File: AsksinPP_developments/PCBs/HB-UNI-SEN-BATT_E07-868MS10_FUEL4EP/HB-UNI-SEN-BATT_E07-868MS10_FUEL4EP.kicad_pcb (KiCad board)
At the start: 2 copper layers, 75 x 75 mm, 30 parts, among them J1 Conn_01x02, J10 charge, J11 ePaper connector, J2 Conn_01x02, J3 Conn_01x02, J4 Conn_01x02, J5 ISP Programmer, J6 Conn_01x04, J7 Conn_01x04, J8 Conn_01x04, J9 Conn_01x04, Q1 IRLU024N, SW1 config button

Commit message: Updates of PCBs/HB-UNI-SEN-BATT_FUEL4EP and HB-UNI-SEN-BATT_E07-868MS10_FUEL4EP
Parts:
- BT1, BT2: footprint FUEL4EP:BATTERY_HOLDER_GOOBAY_AA -> FUEL4EP:BatteryHolder_Keystone_2460_1xAA
- J11: footprint Connector_PinHeader_2.54mm:PinHeader_1x08_P2.54mm_Vertical -> FUEL4EP:PinPads_1x08_P2.00mm_Vertical
- moved BT1 55.3 mm to (164.5, 86.9), turned to 270 degrees
- moved BT2 55.0 mm to (112.4, 138.9), turned to 90 degrees
- moved J11 3.93 mm to (127.9, 130.7)
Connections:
- net Net-(BT1-Pad2) renamed /conBAT
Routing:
- net /D6: track 33.9 -> 47.5 mm, vias 0 -> 2
- net /D7: track 37.6 -> 31.9 mm
- net /SDA: track 101.2 -> 104.3 mm
- net /D5: track 47.5 -> 49.8 mm
- net /SCK: track 76.5 -> 74.6 mm
- net /MISO: track 88.6 -> 87.0 mm
- net /conBAT: track 53.5 -> 52.1 mm
- net /RSET: track 94.8 -> 96.0 mm
- net /MOSI: track 68.1 -> 67.5 mm
- net /plusBAT: track 19.4 -> 19.9 mm
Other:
- board text added: "config"
- board text added: "cut JP2 for accus"
- board text removed: "4"
- board text removed: "5"
- board text removed: "cut JP2 for akkus"

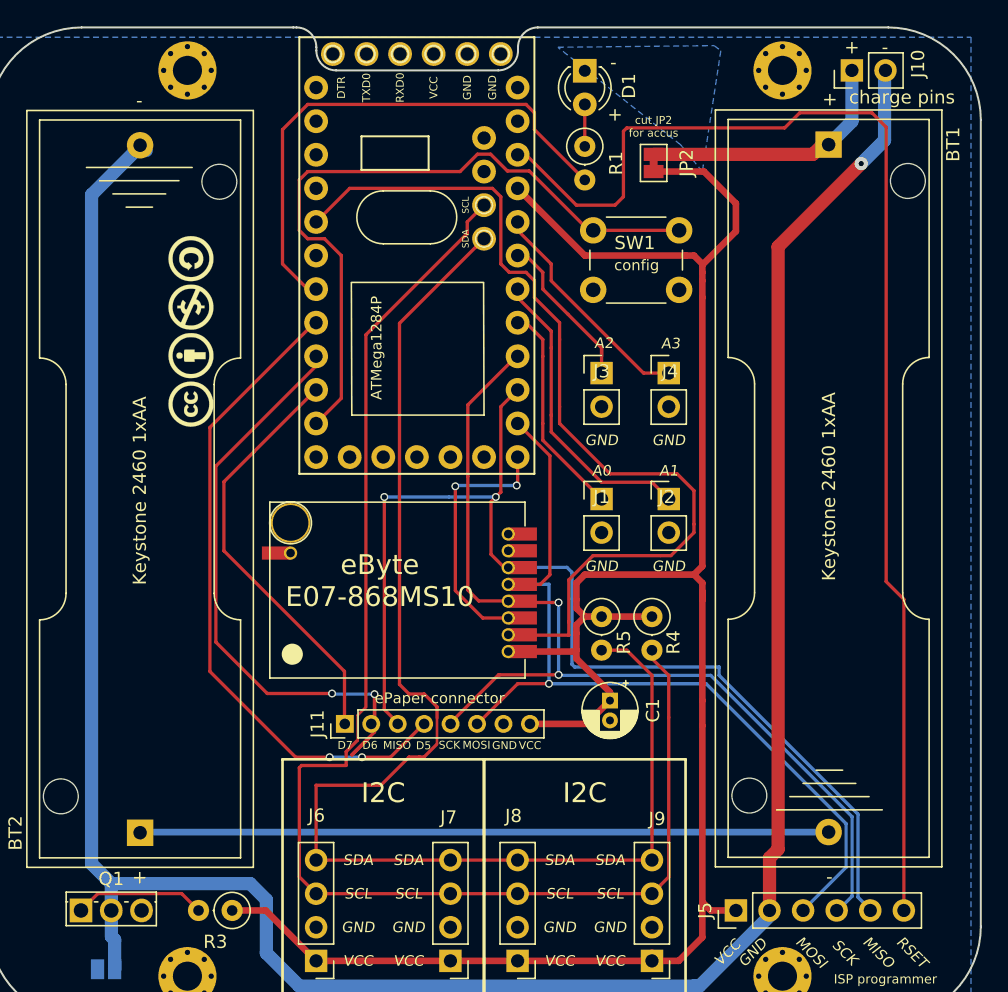
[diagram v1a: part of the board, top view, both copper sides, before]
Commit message: Update of PCBs / added PCBs/HB-UNI-SEN-BATT_ATMega1284P_E07-868MS10_FUEL4EP (all draft only, not yet validated)
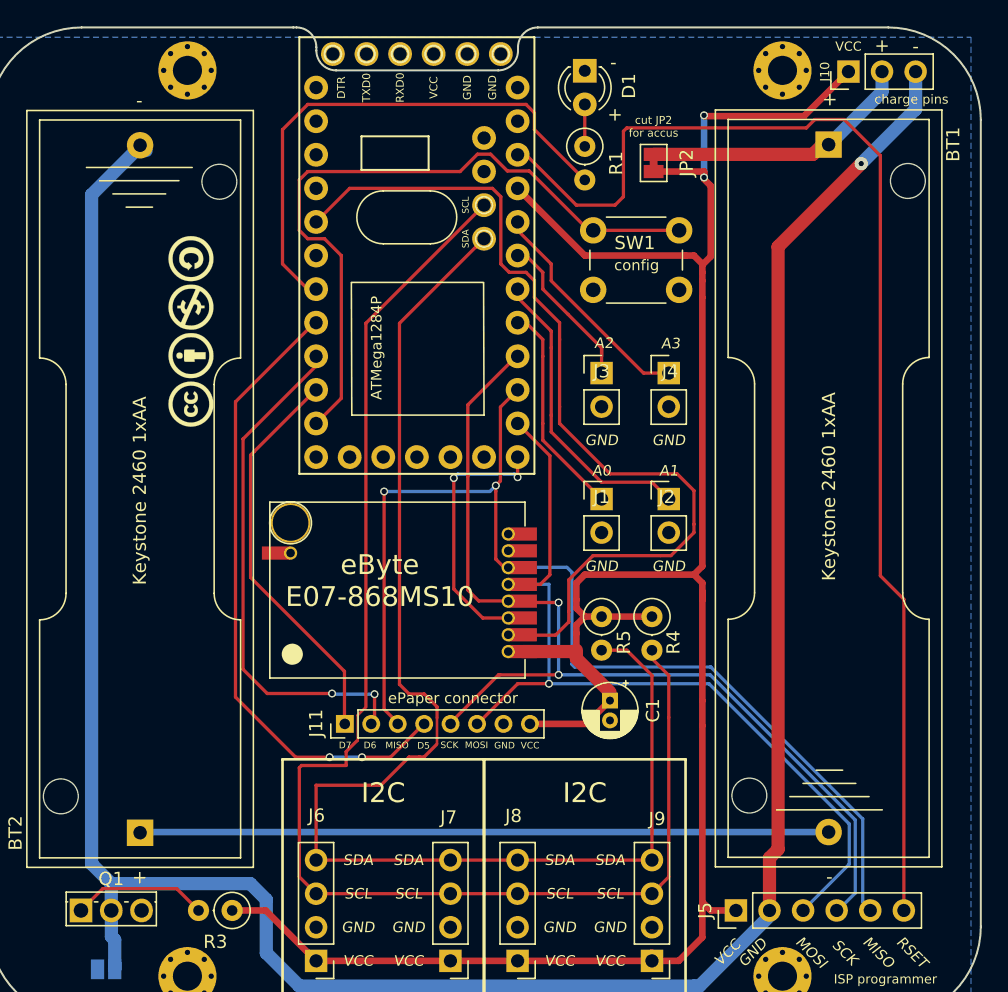
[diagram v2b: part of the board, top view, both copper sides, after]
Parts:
- J10: footprint Connector_PinHeader_2.54mm:PinHeader_1x02_P2.54mm_Vertical -> Connector_PinHeader_2.54mm:PinHeader_1x03_P2.54mm_Vertical
- moved J10 0.28 mm to (166.0, 81.3)
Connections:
- J10 pad 1: /plusBAT -> VCC
- J10 pad 2: /minusBAT -> /plusBAT
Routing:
- net VCC: track 158.9 -> 174.8 mm, vias 0 -> 2
- net /D6: track 47.5 -> 38.6 mm
- net /RSET: track 96.0 -> 94.1 mm
- net /D7: track 31.9 -> 30.2 mm
- net /D5: track 49.8 -> 48.2 mm
- net /plusBAT: track 19.9 -> 20.8 mm
- net /minusBAT: track 190.4 -> 191.4 mm
- net /D2: track 68.7 -> 68.1 mm

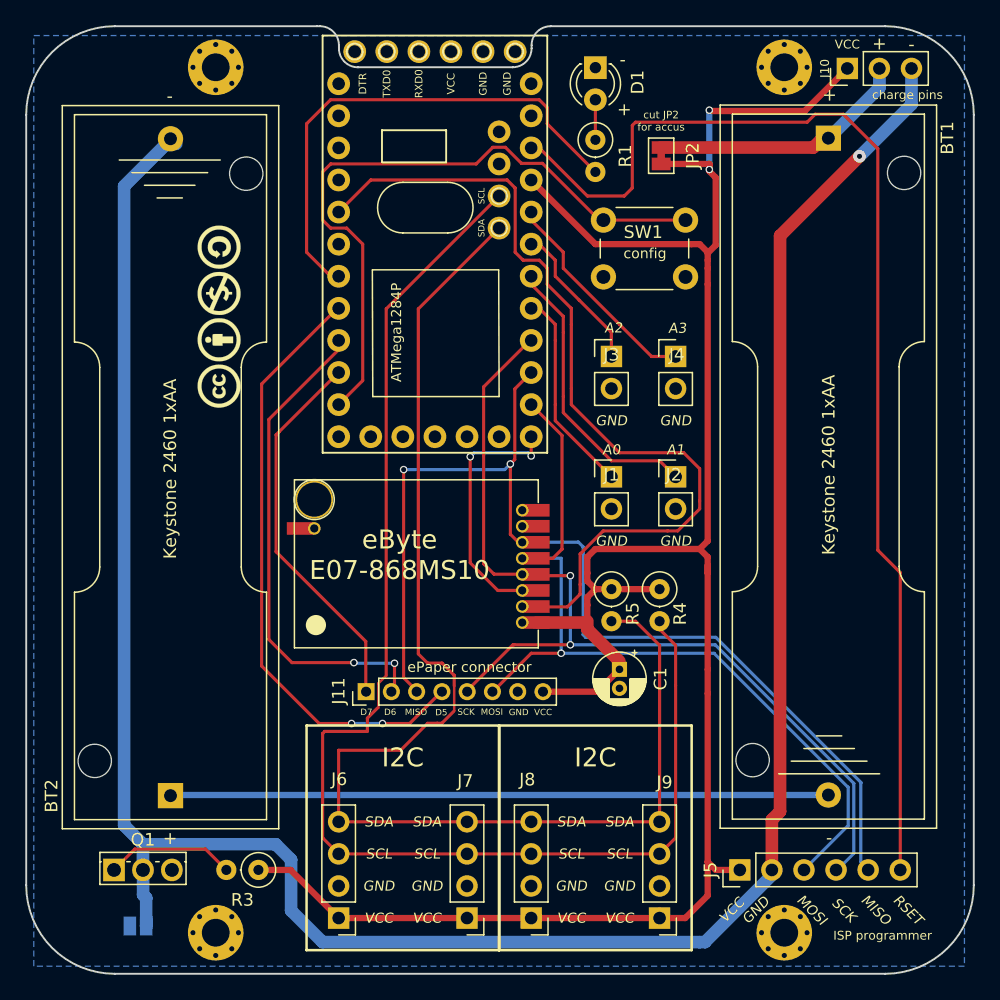
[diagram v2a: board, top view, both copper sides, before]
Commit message: major update: hb-ep-devices-addon V1.14; added sketches HB-UNI-Sensor1-AQ-BME680_KF_rLF and HB-UNI-SenAct-4-4-SC_DS; migration of all PPCBs to KiCAD 6
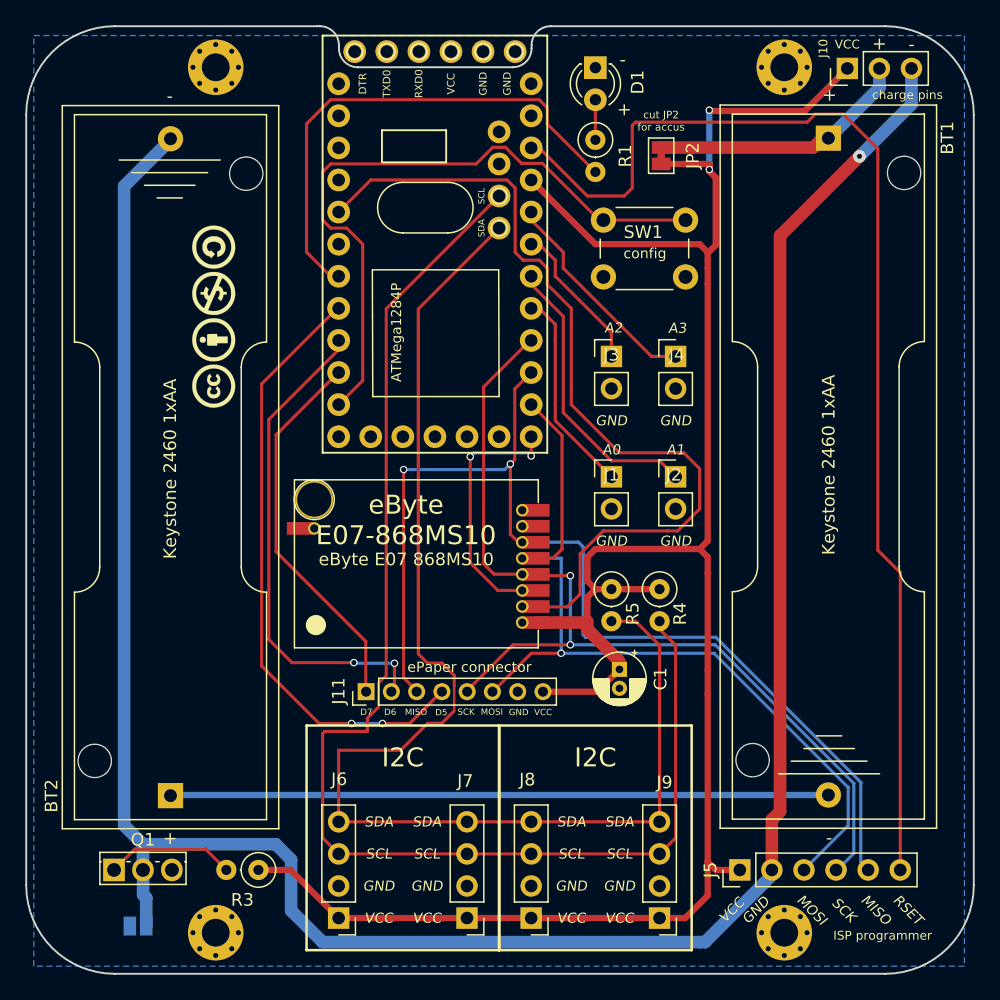
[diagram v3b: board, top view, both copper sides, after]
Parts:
- moved LOGO1 0.43 mm to (115.8, 101.0)
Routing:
- net VCC: track 174.8 -> 172.9 mm
- net /SDA: track 104.3 -> 102.8 mm
- net /minusBAT: track 191.4 -> 190.3 mm
- net /SCK: track 74.8 -> 74.1 mm
- net /A2: track 13.2 -> 12.5 mm
- net /MOSI: track 67.9 -> 67.2 mm
- net /RSET: track 94.1 -> 93.5 mm
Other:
- net class Default removed
- net class battery removed
- net class supply removed
- board text added: "Version 1.1 - 07/2023 (KiCAD 6)"
- board text removed: "Version 1.0 - 10/2021"

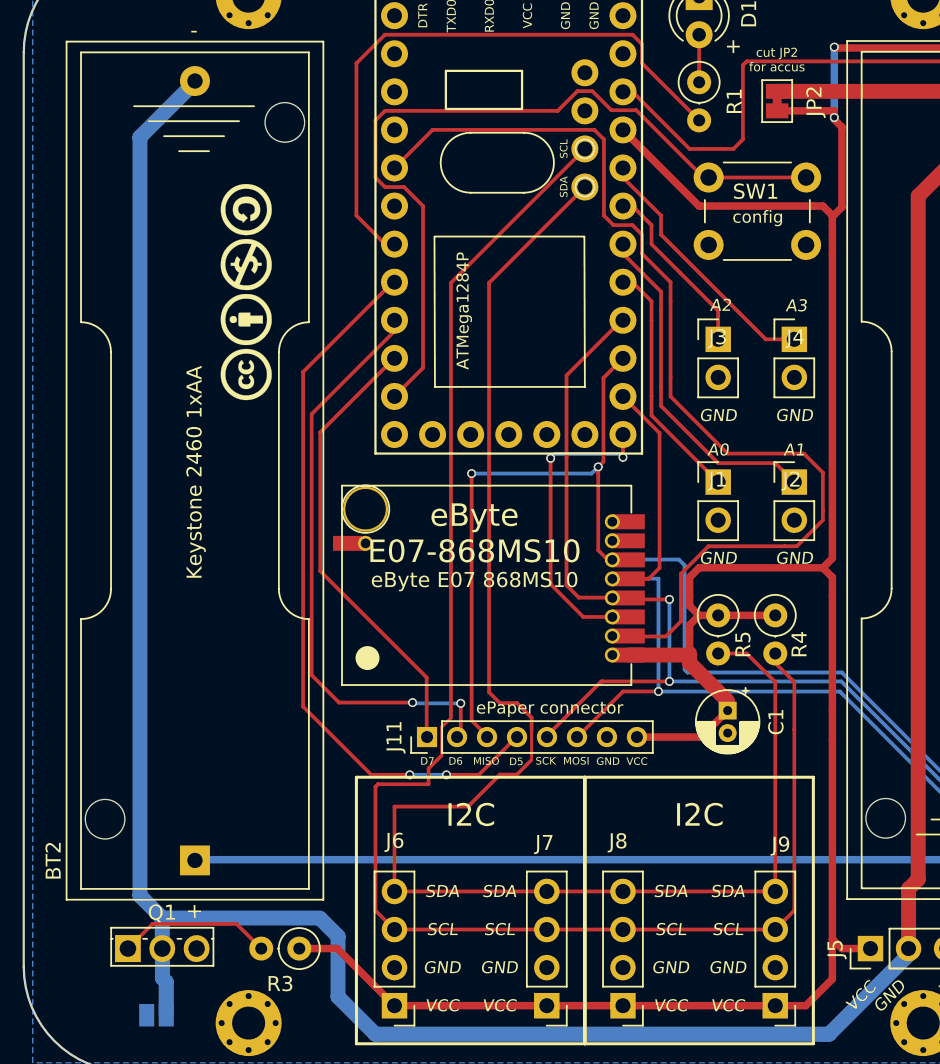
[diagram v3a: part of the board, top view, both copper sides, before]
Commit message: PCBs: KiCAD6 required improvements of layout data bases; added E07-900M10S into FUEL and footprint library
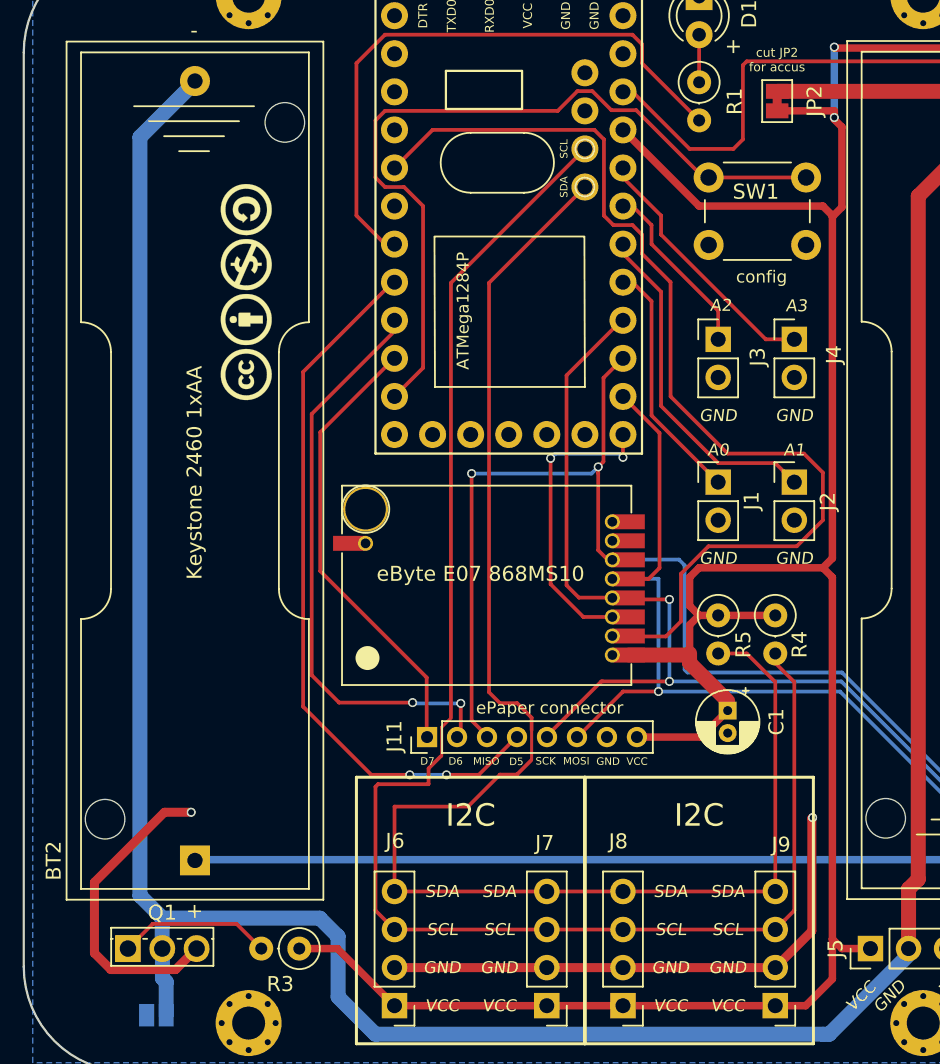
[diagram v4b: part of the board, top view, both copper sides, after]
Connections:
- Module1 pad 2A: Net-(Module1-Pad2A) -> unconnected-(Module1-Pad2A)
- Module1 pad 7C: Net-(Module1-Pad7C) -> unconnected-(Module1-Pad7C)
- Module2 pad 12C: Net-(Module2-Pad12C) -> unconnected-(Module2-Pad12C)
- Module2 pad 1A: Net-(Module2-Pad1A) -> unconnected-(Module2-Pad1A)
- Module2 pad 1B: Net-(Module2-Pad1B) -> unconnected-(Module2-Pad1B)
- Module2 pad 1C: Net-(Module2-Pad1C) -> unconnected-(Module2-Pad1C)
- Module2 pad 1D: Net-(Module2-Pad1D) -> unconnected-(Module2-Pad1D)
- Module2 pad 1E: Net-(Module2-Pad1E) -> unconnected-(Module2-Pad1E)
- Module2 pad 2B: Net-(Module2-Pad2B) -> unconnected-(Module2-Pad2B)
- Module2 pad 2C: Net-(Module2-Pad2C) -> unconnected-(Module2-Pad2C)
- Module2 pad 2D: Net-(Module2-Pad2D) -> unconnected-(Module2-Pad2D)
- Module2 pad 3B: Net-(Module2-Pad3B) -> unconnected-(Module2-Pad3B)
- Module2 pad 3C: Net-(Module2-Pad3C) -> unconnected-(Module2-Pad3C)
- Module2 pad 3D: Net-(Module2-Pad3D) -> unconnected-(Module2-Pad3D)
- Module2 pad 4B: Net-(Module2-Pad4B) -> unconnected-(Module2-Pad4B)
- Module2 pad 4D: Net-(Module2-Pad4D) -> unconnected-(Module2-Pad4D)
- Module2 pad 5B: Net-(Module2-Pad5B) -> unconnected-(Module2-Pad5B)
- Module2 pad 5D: Net-(Module2-Pad5D) -> unconnected-(Module2-Pad5D)
- Module2 pad 6C: Net-(Module2-Pad6C) -> unconnected-(Module2-Pad6C)
- Module2 pad 6D: Net-(Module2-Pad6D) -> unconnected-(Module2-Pad6D)
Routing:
- net GND: track 0.00 -> 57.4 mm, vias 0 -> 2
- net /A2: track 12.5 -> 11.3 mm
- net Net-(Module2-Pad7C): track 40.2 -> 39.6 mm
- net /SCL: track 105.2 -> 104.6 mm
- net /A3: track 17.3 -> 16.6 mm
- net /RSET: track 93.5 -> 92.9 mm
- net /A1: track 22.8 -> 22.2 mm
- net /A0: track 16.3 -> 15.7 mm
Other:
- board text added: "Version 1.2 - 07/2023 (KiCAD 6)"
- board text removed: "Version 1.1 - 07/2023 (KiCAD 6)"
- board text removed: "eByte E07-868MS10"
